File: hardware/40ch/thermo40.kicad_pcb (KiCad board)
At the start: 4 copper layers, 250 x 145 mm, 731 parts, among them J1001 PT100 1-2 (A B C), J1002 PT100 3 (A B C), J101 TC CH1-4, J102 TC CH5-8, J201 TC CH9-12, J202 TC CH13-16, J301 TC CH17-20, J302 TC CH21-24, J401 ENGINE REF FEED/SENSE, J501 AVR ISP, J502 LCD 20x4 HEADER, J503 PANEL BUTTONS, J601 24V IN, J701 TRIP C-NO-NC, J702 ALM C-NO-NC, J703 RS485 A B GND, J801 TC CH25-28, J802 TC CH29-32, J901 TC CH33-36, J902 TC CH37-40, K701 G6K-2F-Y DC5, K702 G6K-2F-Y DC5, Q401 2N7002, Q402 MMBT3906, Q701 2N7002, Q702 2N7002, SW501 UP, SW502 DOWN, SW503 SET, SW504 ESC, SW505 ACK, U1001 AD7124-8BCPZ, U101 AD7124-8BCPZ, U102 TMP126DCKR, U103 TMP126DCKR, U201 AD7124-8BCPZ, U202 TMP126DCKR, U203 TMP126DCKR, U301 AD7124-8BCPZ, U302 TMP126DCKR, U303 TMP126DCKR, U401 B0505S-1WR2, U402 LP2985IM5X-3.3, U403 CA-IS3761HW, U404 CA-IS3761HW, U406 REF3030AIDBZR, U407 MCP6001T-I/OT, U408 TLV7031DBVR, U409 TL431, U410 74HC154, U411 74LVC1G125, U501 ATmega1284P-AU, U601 LM5164DDAR, U703 ADM2587EBRWZ, U801 AD7124-8BCPZ, U802 TMP126DCKR, U803 TMP126DCKR, U901 AD7124-8BCPZ, U902 TMP126DCKR, U903 TMP126DCKR, Y501 8MHz

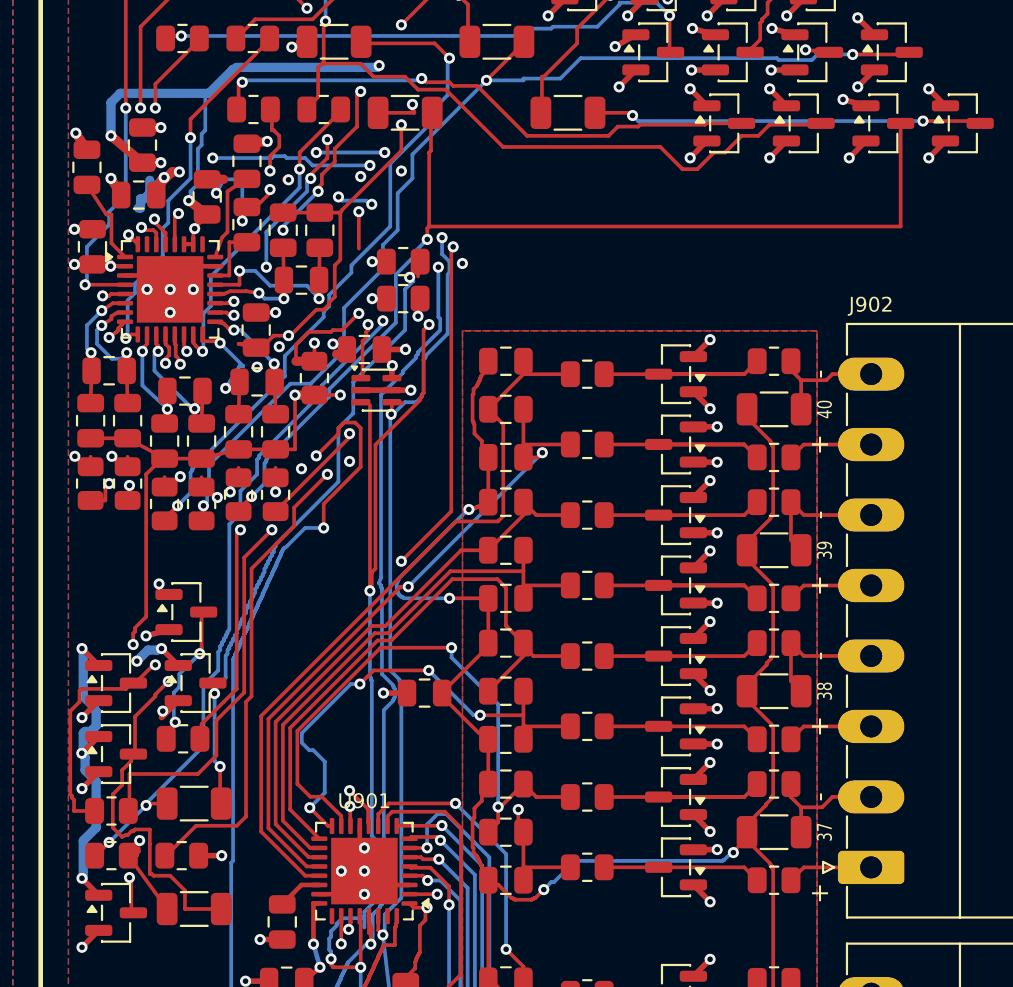
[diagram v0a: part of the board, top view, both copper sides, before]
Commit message: 40ch: Sol round 12 - SAC/SBC adjacent digital crossings 17 -> 0, RTD4_SAC stub removed; re-released 122716
Co-Authored-By: Claude Opus 5.5 <noreply@anthropic.com>
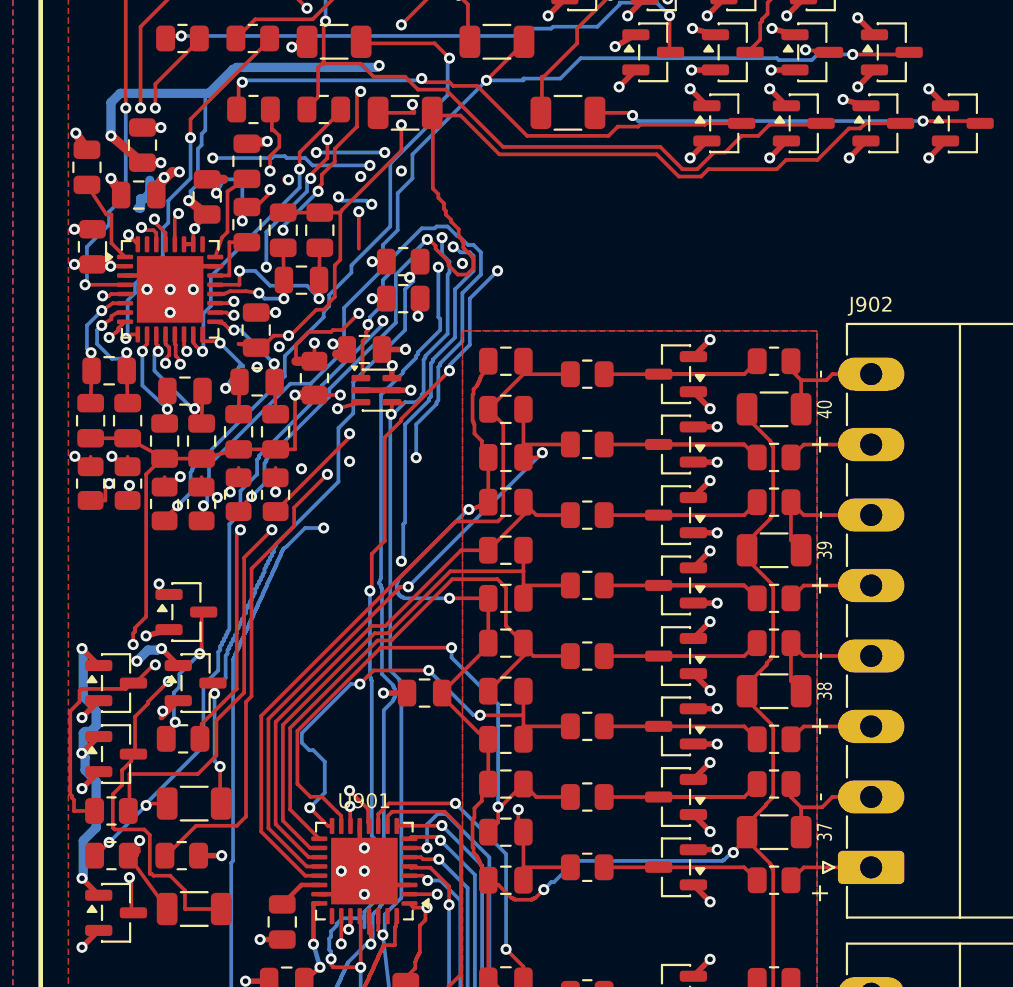
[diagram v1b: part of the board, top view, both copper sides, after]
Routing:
- net CS_CJ10_ISO: track 220.1 -> 228.4 mm
- net DOUT_ISO: track 508.9 -> 515.6 mm, vias 30 -> 32
- net /RTD_1/RTD3_SAC: track 57.0 -> 59.8 mm
- net CS_RTD_ISO: track 230.0 -> 231.3 mm
- net /RTD_1/RTD4_SAC: track 34.7 -> 33.9 mm
